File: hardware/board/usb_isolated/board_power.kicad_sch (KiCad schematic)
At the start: 25 parts

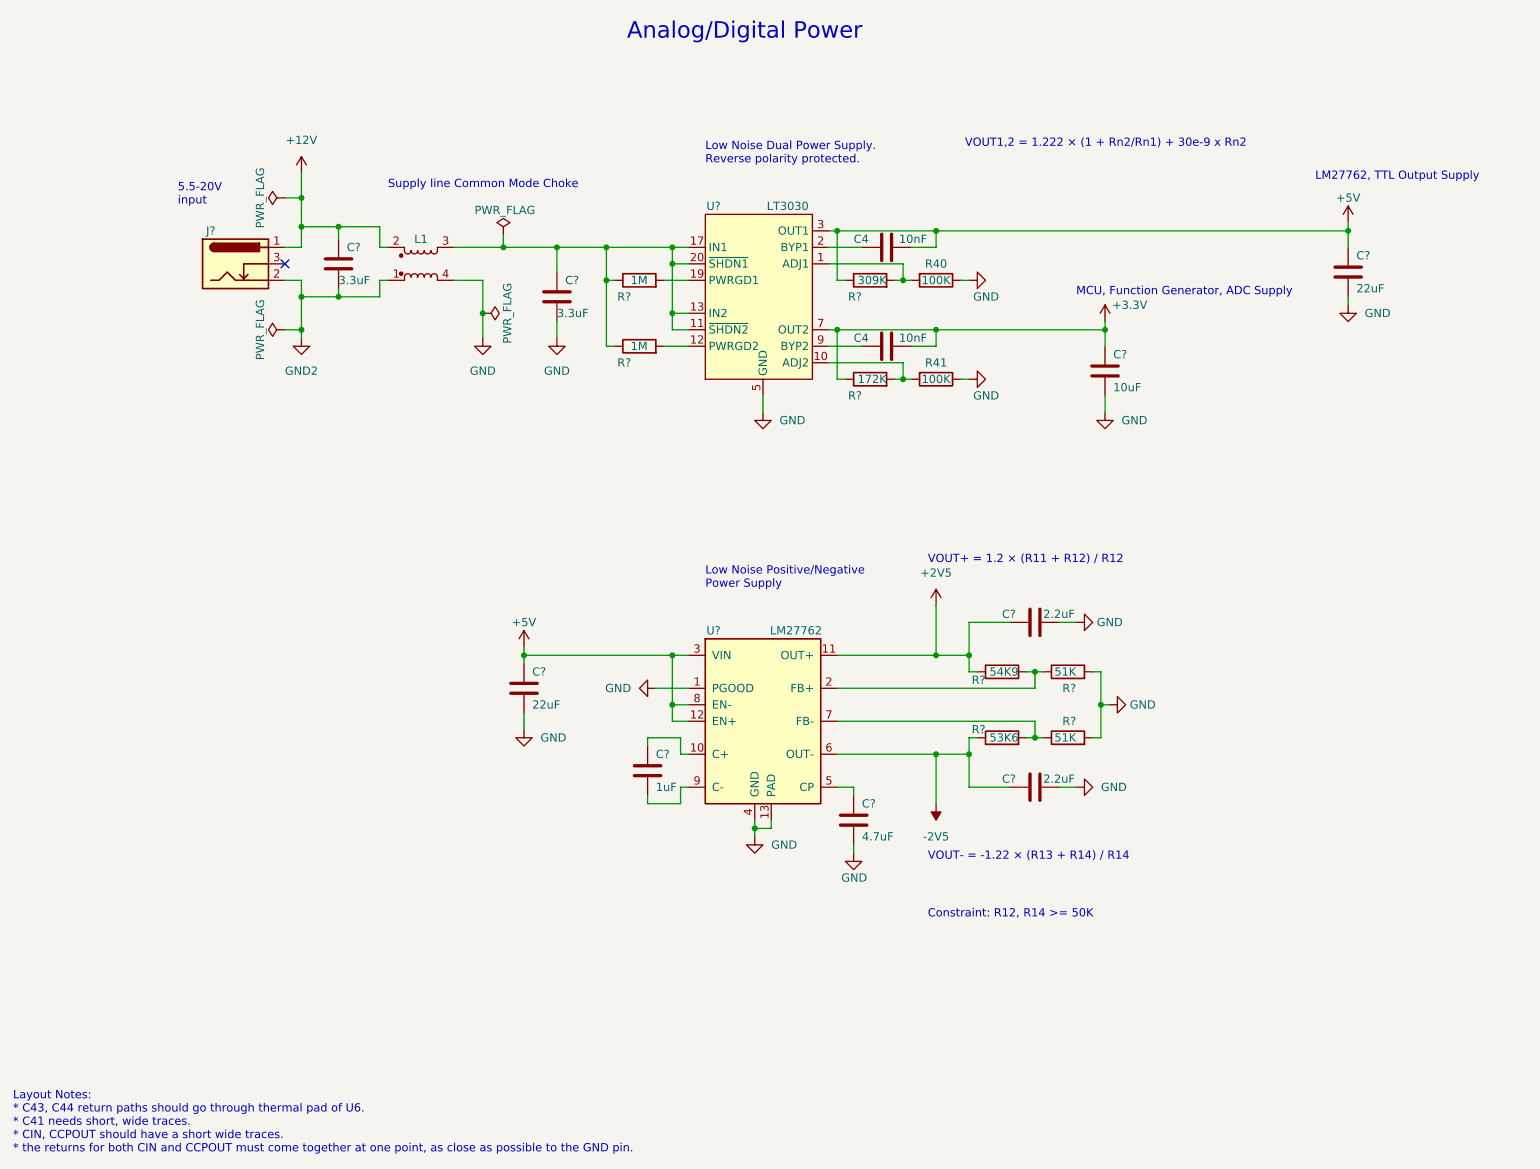
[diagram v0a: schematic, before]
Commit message: update usb isolated pcba layout
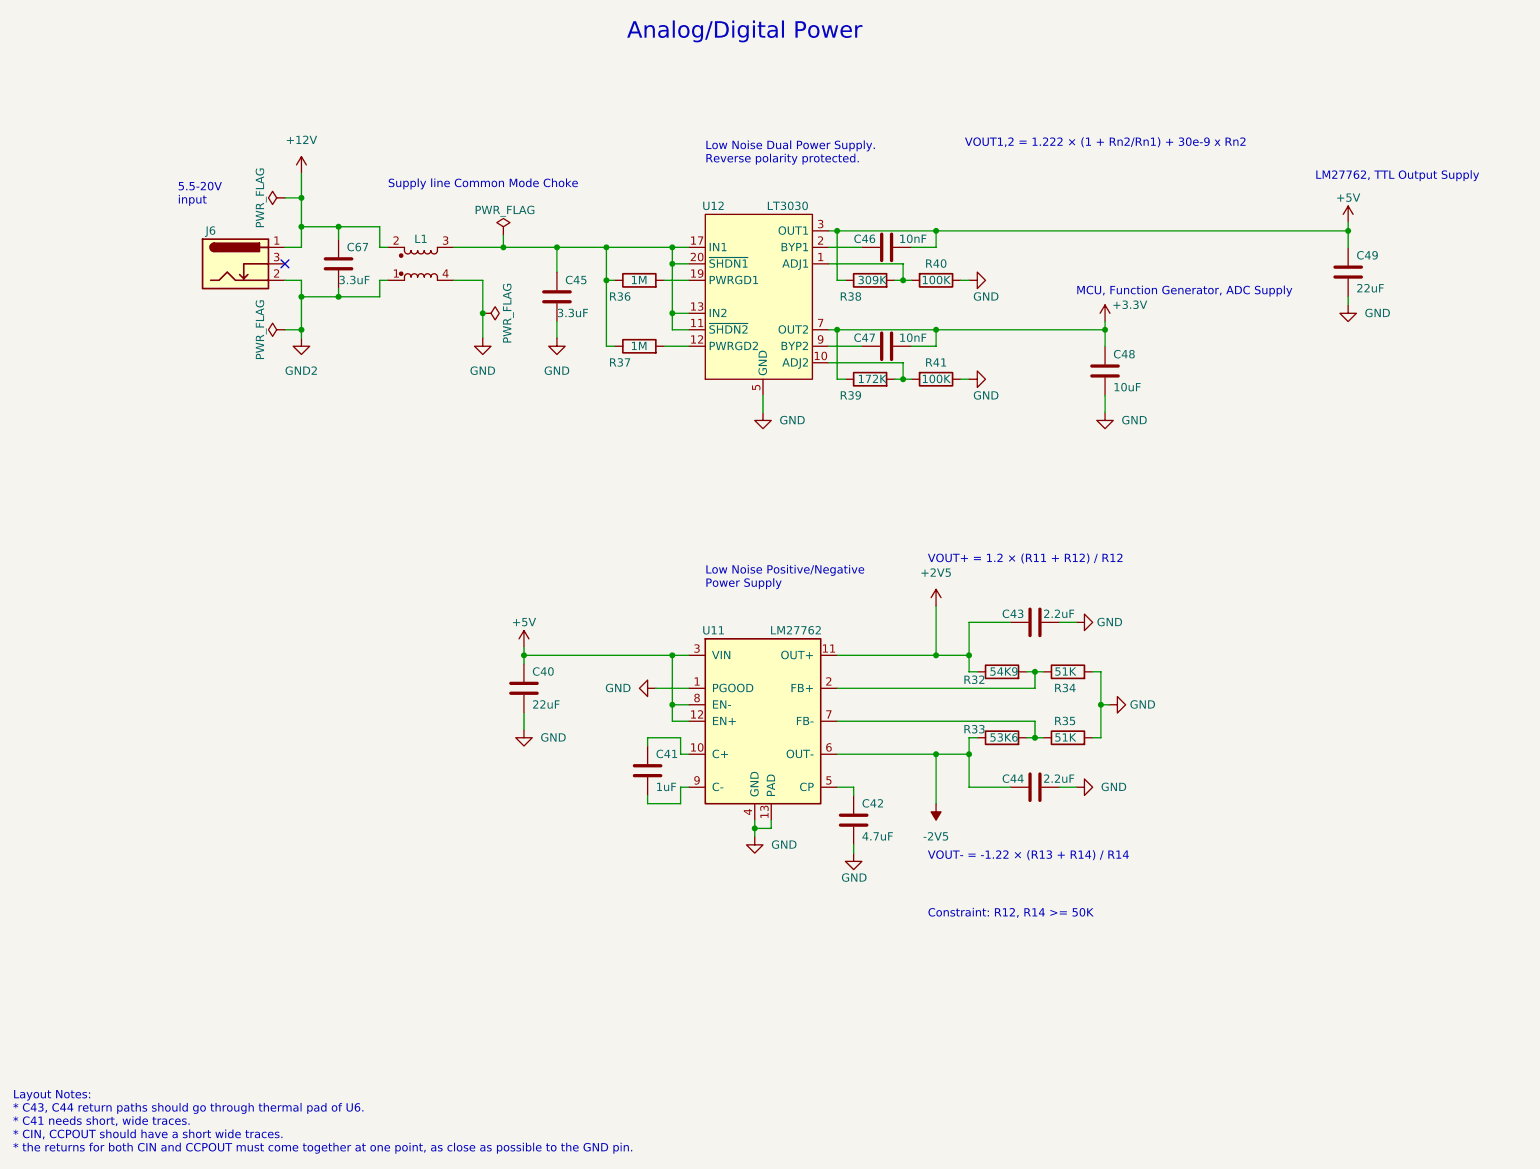
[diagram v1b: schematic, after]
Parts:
- gave numbers to parts that had none: 20
- renumbered C4 to C46, C4 to C47
